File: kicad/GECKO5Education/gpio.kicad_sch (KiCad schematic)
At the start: 4 parts, among them J5 QSE-020-01-XXX-D, U6 LFE5U-85F-6BG381x

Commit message: Made version V1.5
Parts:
- added D1: SBA0530Q_R1_00001, Diode_SMD:D_0402_1005Metric, symbol Device:D
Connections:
- net +5V: now also D1.2 (A)
- net at D124.2 (A), J5.34: no longer J5.32
- new net: D1.1 (K), J5.32
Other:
- moved on the sheet: D124
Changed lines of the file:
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@@
 (kicad_sch (version 20230121) (generator eeschema)
   (paper "A4")
+  (junction (at 127 107.95) (diameter 0) (color 0 0 0 0)
+  )
   (junction (at 95.25 69.85) (diameter 0) (color 0 0 0 0)
   )
   (junction (at 97.79 130.81) (diameter 0) (color 0 0 0 0)
   )
-  (junction (at 95.25 109.22) (diameter 0) (color 0 0 0 0)
-  )
   (junction (at 97.79 128.27) (diameter 0) (color 0 0 0 0)
   )
@@
   (junction (at 97.79 125.73) (diameter 0) (color 0 0 0 0)
   )
+  (wire (pts (xy 127 106.68) (xy 127 107.95))
+    (stroke (width 0) (type default))
+  )
   (wire (pts (xy 95.25 118.11) (xy 97.79 118.11))
     (stroke (width 0) (type default))
@@
     (stroke (width 0) (type default))
   )
+  (wire (pts (xy 127 107.95) (xy 127 110.49))
+    (stroke (width 0) (type default))
+  )
   (wire (pts (xy 200.66 133.35) (xy 204.47 133.35))
     (stroke (width 0) (type default))
@@
     (stroke (width 0) (type default))
   )
-  (wire (pts (xy 95.25 109.22) (xy 95.25 110.49))
-    (stroke (width 0) (type default))
-  )
   (wire (pts (xy 200.66 148.59) (xy 204.47 148.59))
     (stroke (width 0) (type default))
@@
     (stroke (width 0) (type default))
   )
+  (wire (pts (xy 119.38 107.95) (xy 95.25 107.95))
+    (stroke (width 0) (type default))
+  )
   (wire (pts (xy 201.93 95.25) (xy 204.47 95.25))
     (stroke (width 0) (type default))
   )
-  (wire (pts (xy 95.25 107.95) (xy 95.25 109.22))
-    (stroke (width 0) (type default))
-  )
   (wire (pts (xy 95.25 105.41) (xy 97.79 105.41))
     (stroke (width 0) (type default))
   )
+  (wire (pts (xy 119.38 106.68) (xy 119.38 107.95))
+    (stroke (width 0) (type default))
+  )
   (wire (pts (xy 95.25 115.57) (xy 97.79 115.57))
     (stroke (width 0) (type default))
@@
     (stroke (width 0) (type default))
   )
-  (wire (pts (xy 116.84 109.22) (xy 95.25 109.22))
-    (stroke (width 0) (type default))
-  )
   (wire (pts (xy 200.66 115.57) (xy 204.47 115.57))
     (stroke (width 0) (type default))
@@
   )
   (wire (pts (xy 66.04 77.47) (xy 69.85 77.47))
+    (stroke (width 0) (type default))
+  )
+  (wire (pts (xy 95.25 110.49) (xy 119.38 110.49))
     (stroke (width 0) (type default))
   )
@@
     )
   )
-  (symbol (lib_id "power:+5V") (at 124.46 109.22 270) (unit 1)
+  (symbol (lib_id "power:+5V") (at 127 107.95 270) (unit 1)
     (in_bom yes) (on_board yes) (dnp no) (fields_autoplaced)
-    (property "Reference" "#PWR090" (at 120.65 109.22 0)
-      (effects (font (size 1.27 1.27)) hide)
-    )
-    (property "Value" "+5V" (at 128.27 109.855 90)
+    (property "Reference" "#PWR090" (at 123.19 107.95 0)
+      (effects (font (size 1.27 1.27)) hide)
+    )
+    (property "Value" "+5V" (at 130.81 108.585 90)
       (effects (font (size 1.27 1.27)) (justify left))
     )
-    (property "Footprint" "" (at 124.46 109.22 0)
-      (effects (font (size 1.27 1.27)) hide)
-    )
-    (property "Datasheet" "" (at 124.46 109.22 0)
+    (property "Footprint" "" (at 127 107.95 0)
+      (effects (font (size 1.27 1.27)) hide)
+    )
+    (property "Datasheet" "" (at 127 107.95 0)
       (effects (font (size 1.27 1.27)) hide)
     )
@@
     )
   )
+  (symbol (lib_id "Device:D") (at 123.19 106.68 0) (unit 1)
+    (in_bom yes) (on_board yes) (dnp no)
+    (property "Reference" "D1" (at 123.19 104.14 0)
+      (effects (font (size 1.27 1.27)))
+    )
+    (property "Value" "SBA0530Q_R1_00001" (at 123.19 101.6 0)
+      (effects (font (size 1.27 1.27)))
+    )
+    (property "Footprint" "Diode_SMD:D_0402_1005Metric" (at 123.19 106.68 0)
+      (effects (font (size 1.27 1.27)) hide)
+    )
+    (property "Datasheet" "~" (at 123.19 106.68 0)
+      (effects (font (size 1.27 1.27)) hide)
+    )
+    (property "Sim.Device" "D" (at 123.19 106.68 0)
+      (effects (font (size 1.27 1.27)) hide)
+    )
+    (property "Sim.Pins" "1=K 2=A" (at 123.19 106.68 0)
+      (effects (font (size 1.27 1.27)) hide)
+    )
+    (pin "1")
+    (pin "2")
+    (instances
+      (project "gecko5education"
+        (path "/47d58937-9286-45a8-b88f-d3fcc6f916c8/1b790ed2-2ed7-44b0-8848-0151372cb9f5"
+          (reference "D1") (unit 1)
+        )
+        (path "/47d58937-9286-45a8-b88f-d3fcc6f916c8/2168b384-5196-4073-b8ef-3119545e18e5"
+          (reference "D123") (unit 1)
+        )
+      )
+    )
+  )
   (symbol (lib_id "power:GND") (at 97.79 134.62 0) (unit 1)
     (in_bom yes) (on_board yes) (dnp no) (fields_autoplaced)
@@
     )
   )
-  (symbol (lib_id "Device:D") (at 120.65 109.22 180) (unit 1)
-    (in_bom yes) (on_board yes) (dnp no) (fields_autoplaced)
-    (property "Reference" "D124" (at 120.65 102.87 0)
+  (symbol (lib_id "Device:D") (at 123.19 110.49 180) (unit 1)
+    (in_bom yes) (on_board yes) (dnp no)
+    (property "Reference" "D124" (at 123.19 113.03 0)
       (effects (font (size 1.27 1.27)))
     )
-    (property "Value" "SBA0530Q_R1_00001" (at 120.65 105.41 0)
+    (property "Value" "SBA0530Q_R1_00001" (at 123.19 115.57 0)
       (effects (font (size 1.27 1.27)))
     )
-    (property "Footprint" "Diode_SMD:D_0402_1005Metric" (at 120.65 109.22 0)
-      (effects (font (size 1.27 1.27)) hide)
-    )
-    (property "Datasheet" "~" (at 120.65 109.22 0)
-      (effects (font (size 1.27 1.27)) hide)
-    )
-    (property "Sim.Device" "D" (at 120.65 109.22 0)
-      (effects (font (size 1.27 1.27)) hide)
-    )
-    (property "Sim.Pins" "1=K 2=A" (at 120.65 109.22 0)
-      (effects (font (size 1.27 1.27)) hide)
-    )
+    (property "Footprint" "Diode_SMD:D_0402_1005Metric" (at 123.19 110.49 0)
+      (effects (font (size 1.27 1.27)) hide)
+    )
+    (property "Datasheet" "~" (at 123.19 110.49 0)
+      (effects (font (size 1.27 1.27)) hide)
+    )
+    (property "Sim.Device" "D" (at 123.19 110.49 0)
+      (effects (font (size 1.27 1.27)) hide)
+    )
+    (property "Sim.Pins" "1=K 2=A" (at 123.19 110.49 0)
+      (effects (font (size 1.27 1.27)) hide)
+    )

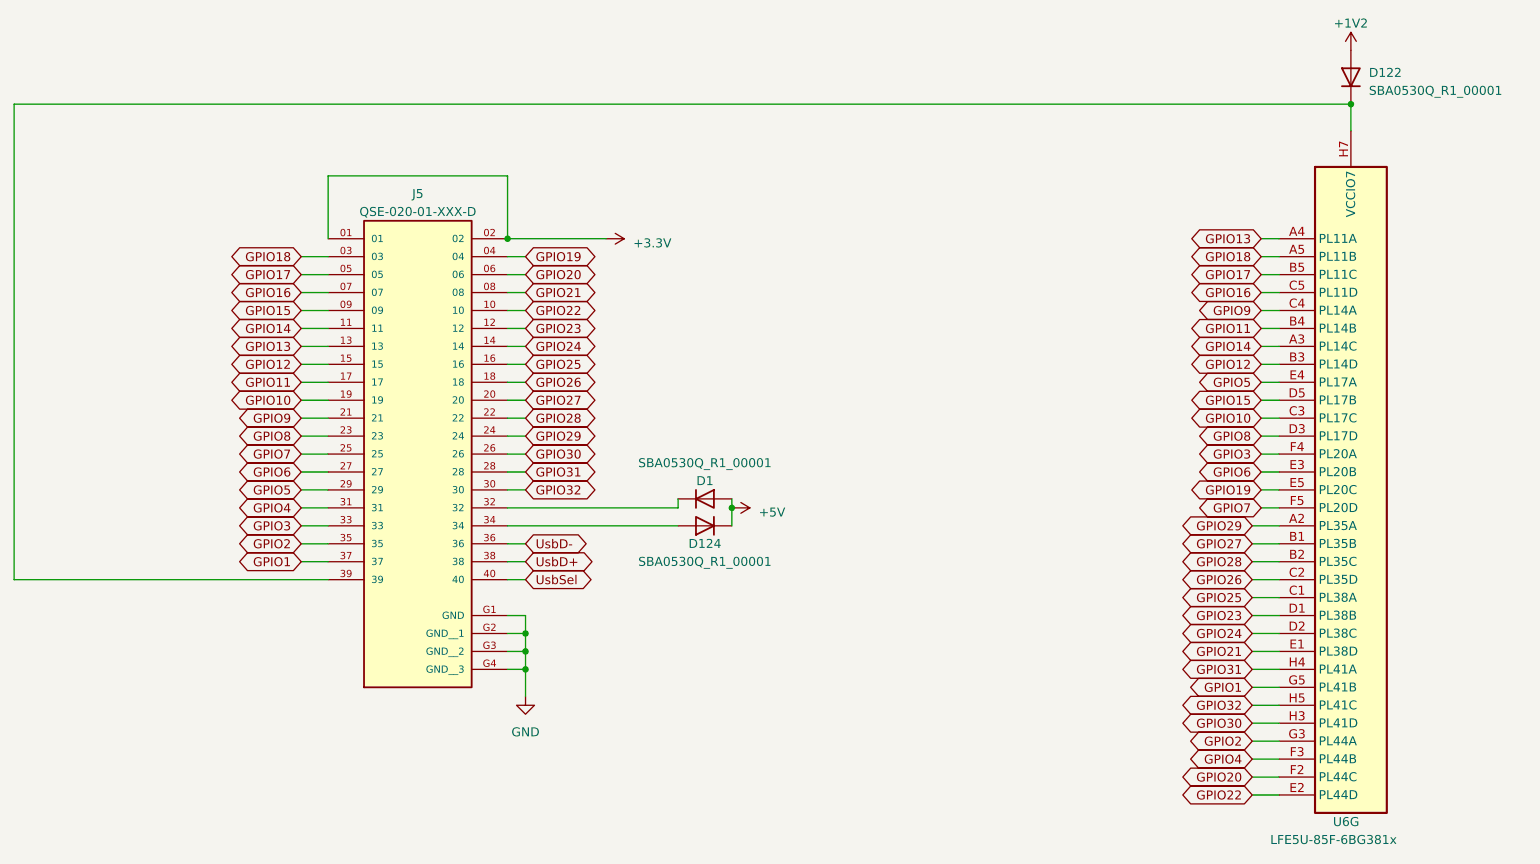
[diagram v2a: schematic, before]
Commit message: Merged perif-add-on to GECKO5
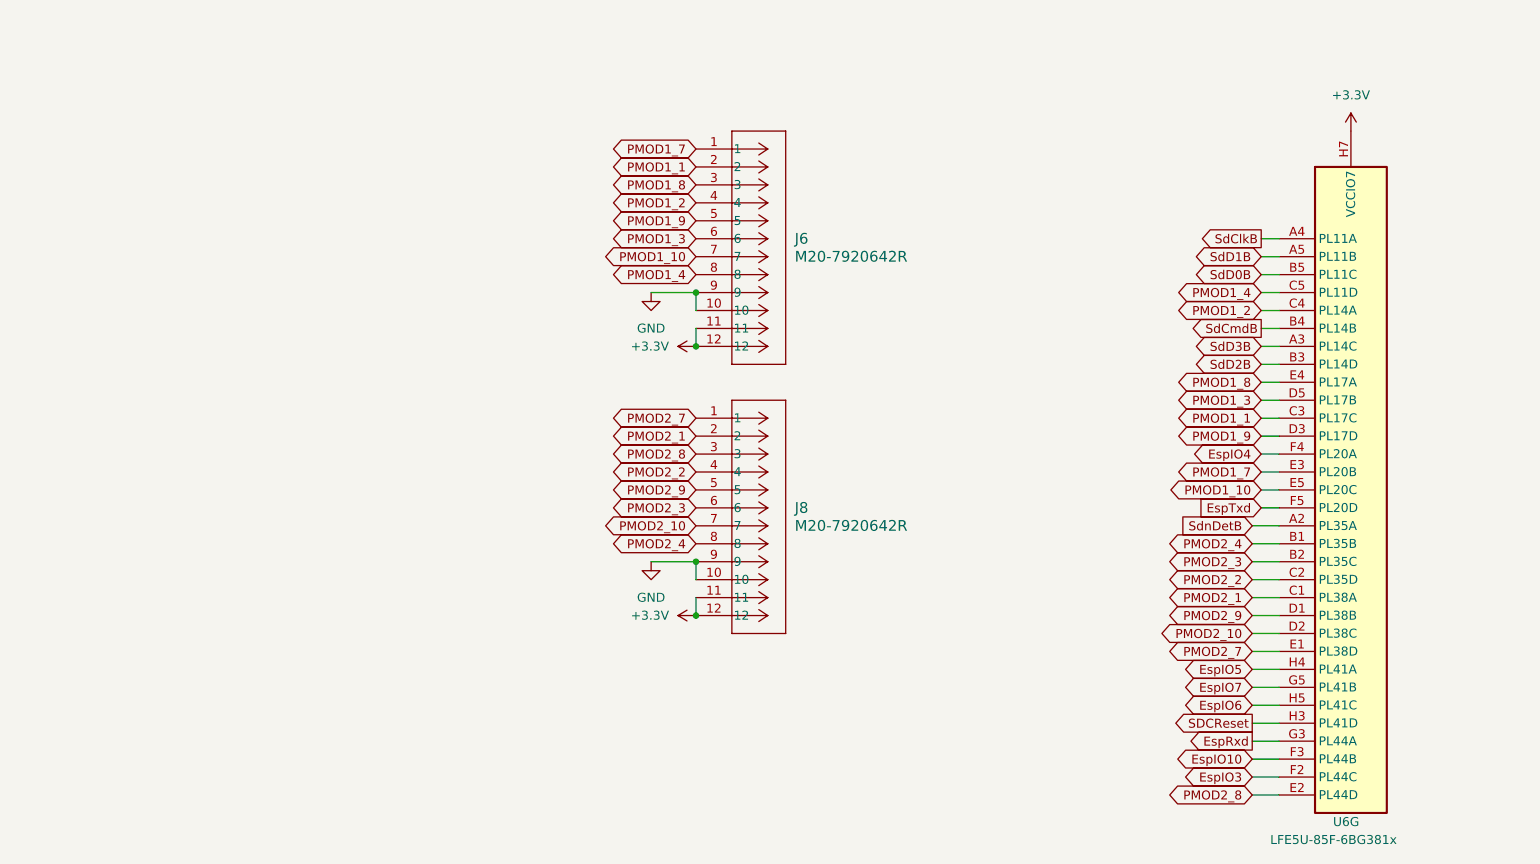
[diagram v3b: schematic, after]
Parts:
- removed D1, D122, D124: SBA0530Q_R1_00001, Diode_SMD:D_0402_1005Metric, symbol Device:D
- removed J5: QSE-020-01-XXX-D, gecko4education:SAMTEC_QSE-020-01-X-D-A, symbol gecko5education:QSE-020-01-XXX-D
- added J6, J8: M20-7920642R, gecko4education:CONN_M20-7920642R_HRW, symbol gecko5education:M20-7920642R
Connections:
- net +3.3V: now also U6.H6 (VCCIO7), U6.H7 (VCCIO7), U6.J6 (VCCIO7), J6.11, J6.12, J8.11, J8.12
- net GND: now also J6.10, J6.9, J8.10, J8.9
- net GPIO1 renamed EspIO7
- net GPIO10 renamed PMOD1_1
- net PMOD1_1: now also J6.2
- net GPIO11 renamed SdCmdB
- net GPIO12 renamed SdD2B
- net GPIO13 renamed SdClkB
- net GPIO14 renamed SdD3B
- net GPIO15 renamed PMOD1_3
- net PMOD1_3: now also J6.6
- net GPIO16 renamed PMOD1_4
- net PMOD1_4: now also J6.8
- net GPIO17 renamed SdD0B
- net GPIO18 renamed SdD1B
- net GPIO19 renamed PMOD1_10
- net PMOD1_10: now also J6.7
- net GPIO2 renamed EspRxd
- net GPIO20 renamed EspIO3
- net GPIO21 renamed PMOD2_7
- net PMOD2_7: now also J8.1
- net GPIO22 renamed PMOD2_8
- net PMOD2_8: now also J8.3
- net GPIO23 renamed PMOD2_9
- net PMOD2_9: now also J8.5
- net GPIO24 renamed PMOD2_10
- net PMOD2_10: now also J8.7
- net GPIO25 renamed PMOD2_1
- net PMOD2_1: now also J8.2
- net GPIO26 renamed PMOD2_2
- net PMOD2_2: now also J8.4
- net GPIO27 renamed PMOD2_4
- net PMOD2_4: now also J8.8
- net GPIO28 renamed PMOD2_3
- net PMOD2_3: now also J8.6
- net GPIO29 renamed SdnDetB
- net GPIO3 renamed EspIO4
- net GPIO30 renamed SDCReset
- net GPIO31 renamed EspIO5
- net GPIO32 renamed EspIO6
- net GPIO4 renamed EspIO10
- net GPIO5 renamed PMOD1_8
- net PMOD1_8: now also J6.3
- net GPIO6 renamed PMOD1_7
- net PMOD1_7: now also J6.1
- net GPIO7 renamed EspTxd
- net GPIO8 renamed PMOD1_9
- net PMOD1_9: now also J6.5
- net GPIO9 renamed PMOD1_2
- net PMOD1_2: now also J6.4

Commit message: Prototype Version V3.0
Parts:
- added J9: Phoenix 1156943, gecko4education:PHOENIX_1156943, symbol Connector_Generic:Conn_02x15_Odd_Even
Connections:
- net GND: now also J9.19 (Pin_19), J9.20 (Pin_20), J9.24 (Pin_24), J9.25 (Pin_25), J9.26 (Pin_26), J9.28 (Pin_28), J9.30 (Pin_30)
- net PMOD1_1: now also J9.10 (Pin_10)
- net PMOD1_10: now also J9.15 (Pin_15)
- net PMOD1_2: now also J9.12 (Pin_12)
- net PMOD1_3: now also J9.14 (Pin_14)
- net PMOD1_4: now also J9.16 (Pin_16)
- net PMOD1_7: now also J9.9 (Pin_9)
- net PMOD1_8: now also J9.11 (Pin_11)
- net PMOD1_9: now also J9.13 (Pin_13)
- net PMOD2_1: now also J9.2 (Pin_2)
- net PMOD2_10: now also J9.7 (Pin_7)
- net PMOD2_2: now also J9.4 (Pin_4)
- net PMOD2_3: now also J9.6 (Pin_6)
- net PMOD2_4: now also J9.8 (Pin_8)
- net PMOD2_7: now also J9.1 (Pin_1)
- net PMOD2_8: now also J9.3 (Pin_3)
- net PMOD2_9: now also J9.5 (Pin_5)
- new net ADC_ChanA: J9.21 (Pin_21)
- new net ADC_ChanB: J9.22 (Pin_22)
- new net DAC_ChanA: J9.27 (Pin_27)
- new net DAC_ChanB: J9.29 (Pin_29)
- new net VREF: J9.23 (Pin_23)
- no-connect marks 0 -> 2
